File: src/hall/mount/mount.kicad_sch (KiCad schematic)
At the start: 58 parts, among them J1 01x04 Male, J2 01x02 Male, J3 01x03 Male, J4 PJ398SM, J5 PJ398SM, J6 PJ398SM, J7 PJ398SM, Q1 MMBT3904, Q2 MMBT3904, Q3 MMBT3904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

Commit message: update to Kicad8
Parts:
- H1, H2, H3, H4: now left out of the parts list

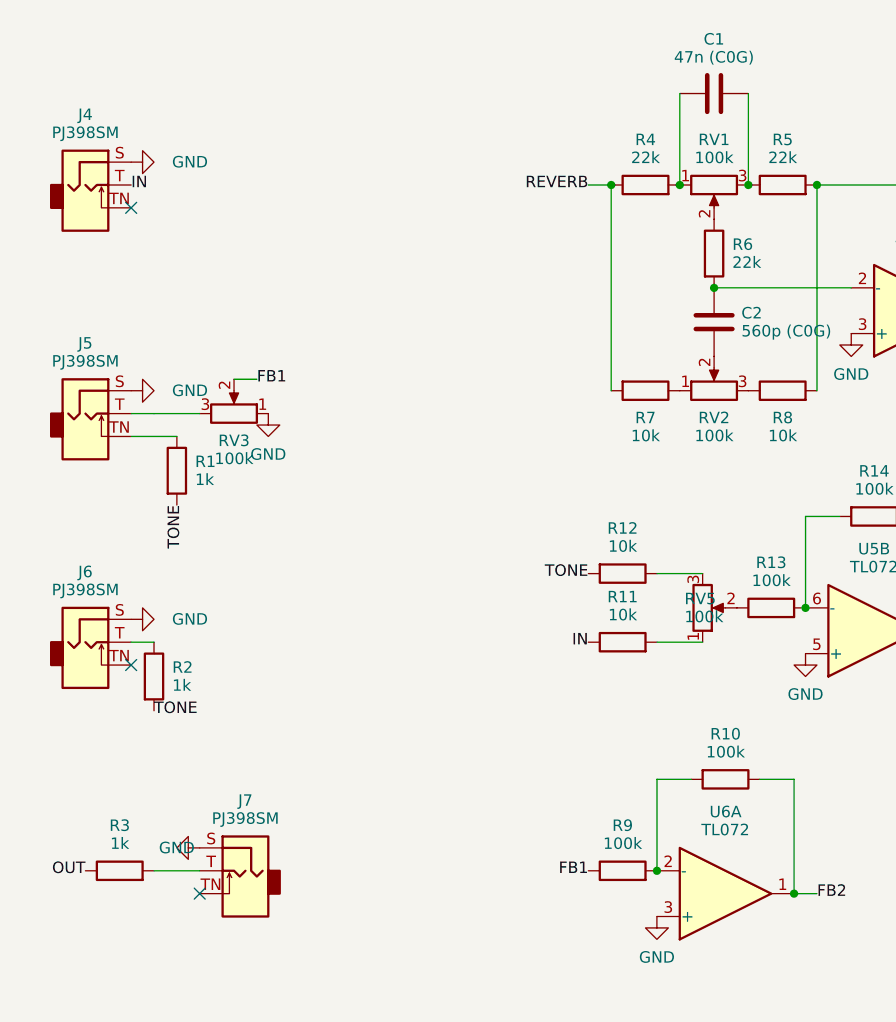
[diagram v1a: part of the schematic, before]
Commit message: update to latest elektron version
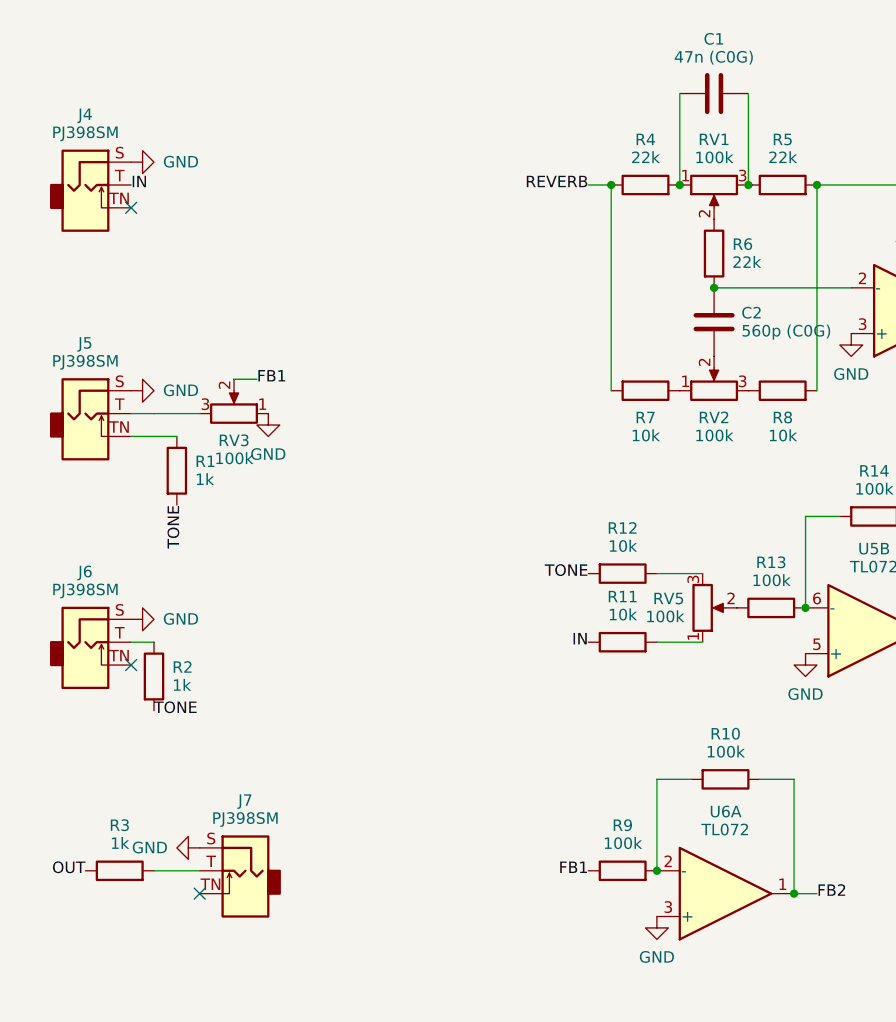
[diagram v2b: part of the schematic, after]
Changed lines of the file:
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@@
     (property "Reference" "GND" (at 0 -6.35 0) (effects (font (size 1.27 1.27))
         (hide yes)))
-    (property "Value" "GND" (at 29.94 48.26 90) (effects (font (size 1.27 1.27)) (justify right)))
+    (property "Value" "GND" (at 28.94 48.260000000000005 -90) (effects (font (size 1.27 1.27)) (justify left)))
     (property "Footprint" "" (at 0 0 0) (effects (font (size 1.27 1.27))
         (hide yes)))
@@
     (property "Reference" "GND" (at 0 -6.35 0) (effects (font (size 1.27 1.27))
         (hide yes)))
-    (property "Value" "GND" (at 29.94 73.66 90) (effects (font (size 1.27 1.27)) (justify right)))
+    (property "Value" "GND" (at 28.94 73.66 -90) (effects (font (size 1.27 1.27)) (justify left)))
     (property "Footprint" "" (at 0 0 0) (effects (font (size 1.27 1.27))
         (hide yes)))
@@
     (property "ki_fp_filters" "Potentiometer*" (at 0 0 0) (effects (font (size 1.27 1.27))
         (hide yes)))
+    (property "Spice_Primitive" "X" (at 36.83 76.2 0) (effects (font (size 1.27 1.27)) hide))
     (property "Spice_Model" "Potentiometer" (at 36.83 76.2 0) (effects (font (size 1.27 1.27)) hide))
-    (property "Spice_Primitive" "X" (at 36.83 76.2 0) (effects (font (size 1.27 1.27)) hide))
   )
   (wire
@@
     (property "Reference" "GND" (at 0 -6.35 0) (effects (font (size 1.27 1.27))
         (hide yes)))
-    (property "Value" "GND" (at 29.94 99.06 90) (effects (font (size 1.27 1.27)) (justify right)))
+    (property "Value" "GND" (at 28.94 99.06 -90) (effects (font (size 1.27 1.27)) (justify left)))
     (property "Footprint" "" (at 0 0 0) (effects (font (size 1.27 1.27))
         (hide yes)))
@@
     (property "Reference" "GND" (at 0 -6.35 0) (effects (font (size 1.27 1.27))
         (hide yes)))
-    (property "Value" "GND" (at 28.48 124.46 -270) (effects (font (size 1.27 1.27)) (justify left)))
+    (property "Value" "GND" (at 29.48 124.46000000000001 -270) (effects (font (size 1.27 1.27)) (justify right)))
     (property "Footprint" "" (at 0 0 0) (effects (font (size 1.27 1.27))
         (hide yes)))
@@
     (property "ki_fp_filters" "Potentiometer*" (at 0 0 0) (effects (font (size 1.27 1.27))
         (hide yes)))
+    (property "Spice_Primitive" "X" (at 90.17 50.8 0) (effects (font (size 1.27 1.27)) hide))
     (property "Spice_Netlist_Enabled" "Y" (at 90.17 50.8 0) (effects (font (size 1.27 1.27)) hide))
     (property "Spice_Model" "Potentiometer" (at 90.17 50.8 0) (effects (font (size 1.27 1.27)) hide))
-    (property "Spice_Primitive" "X" (at 90.17 50.8 0) (effects (font (size 1.27 1.27)) hide))
   )
   (junction (at 93.98 50.8)
@@
     (property "ki_fp_filters" "SOIC*3.9x4.9mm*P1.27mm* DIP*W7.62mm* TO*99* OnSemi*Micro8* TSSOP*3x3mm*P0.65mm* TSSOP*4.4x3mm*P0.65mm* MSOP*3x3mm*P0.65mm* SSOP*3.9x4.9mm*P0.635mm* LFCSP*2x2mm*P0.5mm* *SIP* SOIC*5.3x6.2mm*P1.27mm*" (at 0 0 0) (effects (font (size 1.27 1.27))
         (hide yes)))
+    (property "Spice_Model" "TL072c" (at 113.03 64.77 0) (effects (font (size 1.27 1.27)) hide))
     (property "Spice_Primitive" "X" (at 113.03 64.77 0) (effects (font (size 1.27 1.27)) hide))
-    (property "Spice_Model" "TL072c" (at 113.03 64.77 0) (effects (font (size 1.27 1.27)) hide))
   )
   (symbol (lib_id "power:GND") (at 105.41 67.31 0)
@@
     (property "ki_fp_filters" "SOIC*3.9x4.9mm*P1.27mm* DIP*W7.62mm* TO*99* OnSemi*Micro8* TSSOP*3x3mm*P0.65mm* TSSOP*4.4x3mm*P0.65mm* MSOP*3x3mm*P0.65mm* SSOP*3.9x4.9mm*P0.635mm* LFCSP*2x2mm*P0.5mm* *SIP* SOIC*5.3x6.2mm*P1.27mm*" (at 0 0 0) (effects (font (size 1.27 1.27))
         (hide yes)))
+    (property "Spice_Primitive" "X" (at 91.44 129.54 0) (effects (font (size 1.27 1.27)) hide))
     (property "Spice_Model" "TL072c" (at 91.44 129.54 0) (effects (font (size 1.27 1.27)) hide))
-    (property "Spice_Primitive" "X" (at 91.44 129.54 0) (effects (font (size 1.27 1.27)) hide))
   )
   (symbol (lib_id "power:GND") (at 83.82 132.08 0)
@@
     (unit 1)
     (exclude_from_sim no) (in_bom yes) (on_board yes)
-    (property "Reference" "RV5" (at 86.88 96.78999999999999 0) (effects (font (size 1.27 1.27)) (justify left)))
-    (property "Value" "100k" (at 86.88 98.78999999999999 0) (effects (font (size 1.27 1.27)) (justify left)))
+    (property "Reference" "RV5" (at 86.88 96.78999999999999 0) (effects (font (size 1.27 1.27)) (justify right)))
+    (property "Value" "100k" (at 86.88 98.78999999999999 0) (effects (font (size 1.27 1.27)) (justify right)))
     (property "Footprint" elektrophon:Potentiometer_Alpha_RD901F-40-00D_Single_Vertical (at 0 0 0) (effects (font (size 1.27 1.27))
         (hide yes) hide))
@@
     (property "ki_fp_filters" "Potentiometer*" (at 0 0 0) (effects (font (size 1.27 1.27))
         (hide yes)))
+    (property "Spice_Netlist_Enabled" "Y" (at 88.9 97.79 0) (effects (font (size 1.27 1.27)) hide))
+    (property "Spice_Primitive" "X" (at 88.9 97.79 0) (effects (font (size 1.27 1.27)) hide))
     (property "Spice_Model" "Potentiometer1" (at 88.9 97.79 0) (effects (font (size 1.27 1.27)) hide))
-    (property "Spice_Primitive" "X" (at 88.9 97.79 0) (effects (font (size 1.27 1.27)) hide))
-    (property "Spice_Netlist_Enabled" "Y" (at 88.9 97.79 0) (effects (font (size 1.27 1.27)) hide))
   )
   (wire
@@
     (property "ki_fp_filters" "SOIC*3.9x4.9mm*P1.27mm* DIP*W7.62mm* TO*99* OnSemi*Micro8* TSSOP*3x3mm*P0.65mm* TSSOP*4.4x3mm*P0.65mm* MSOP*3x3mm*P0.65mm* SSOP*3.9x4.9mm*P0.635mm* LFCSP*2x2mm*P0.5mm* *SIP* SOIC*5.3x6.2mm*P1.27mm*" (at 0 0 0) (effects (font (size 1.27 1.27))
         (hide yes)))
+    (property "Spice_Model" "TL072c" (at 107.95 100.33 0) (effects (font (size 1.27 1.27)) hide))
     (property "Spice_Primitive" "X" (at 107.95 100.33 0) (effects (font (size 1.27 1.27)) hide))
-    (property "Spice_Model" "TL072c" (at 107.95 100.33 0) (effects (font (size 1.27 1.27)) hide))
   )
   (symbol (lib_id "power:GND") (at 100.33 102.87 0)
@@
     (property "ki_fp_filters" "SOIC*3.9x4.9mm*P1.27mm* DIP*W7.62mm* TO*99* OnSemi*Micro8* TSSOP*3x3mm*P0.65mm* TSSOP*4.4x3mm*P0.65mm* MSOP*3x3mm*P0.65mm* SSOP*3.9x4.9mm*P0.635mm* LFCSP*2x2mm*P0.5mm* *SIP* SOIC*5.3x6.2mm*P1.27mm*" (at 0 0 0) (effects (font (size 1.27 1.27))
         (hide yes)))
+    (property "Spice_Model" "TL072c" (at 81.28 190.5 0) (effects (font (size 1.27 1.27)) hide))
     (property "Spice_Primitive" "X" (at 81.28 190.5 0) (effects (font (size 1.27 1.27)) hide))
-    (property "Spice_Model" "TL072c" (at 81.28 190.5 0) (effects (font (size 1.27 1.27)) hide))
   )
   (symbol (lib_id "power:GND") (at 73.66 193.04 0)
